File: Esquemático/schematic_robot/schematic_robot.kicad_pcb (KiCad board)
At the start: 2 copper layers, 19 parts, among them J1 Conn_01x04_Pin, J2 Conn_01x01_Socket, J3 Conn_01x01_Socket, J4 Conn_01x01_Socket, J5 Conn_01x01_Socket, J6 Conn_01x01_Socket, J7 Conn_01x01_Socket, J8 Conn_01x01_Socket, J9 Conn_01x01_Socket, M1 Motor_Servo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

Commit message: canseira
eu ein
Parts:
- moved J9 18.4 mm to (97.5, 109.0)
- moved J2 16.7 mm to (88.0, 93.0)
- moved J3 15.5 mm to (86.5, 108.0)
- moved J4 12.5 mm to (101.0, 91.0)
- moved J6 11.6 mm to (100.0, 99.0)
- moved J7 8.66 mm to (114.0, 115.0)
- moved J5 7.83 mm to (105.0, 114.5)
- moved J8 4.14 mm to (112.0, 104.0)
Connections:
- net +12V renamed 12V
- J3 pad 1: Net-(J3-Pin_1) -> 5V
- J8 pad 1: Net-(J8-Pin_1) -> 5V
- M1 pad 2: Net-(J3-Pin_1) -> 5V
- M2 pad 2: Net-(J3-Pin_1) -> 5V
- M3 pad 2: Net-(J3-Pin_1) -> 5V
- M4 pad 2: Net-(J3-Pin_1) -> 5V
- M5 pad 2: Net-(J3-Pin_1) -> 5V
- R1 pad 1: +5V -> 5V
- R2 pad 1: +5V -> 5V
- U2 pad 2: Net-(J8-Pin_1) -> 5V
- U3 pad 14: +5V -> 5V

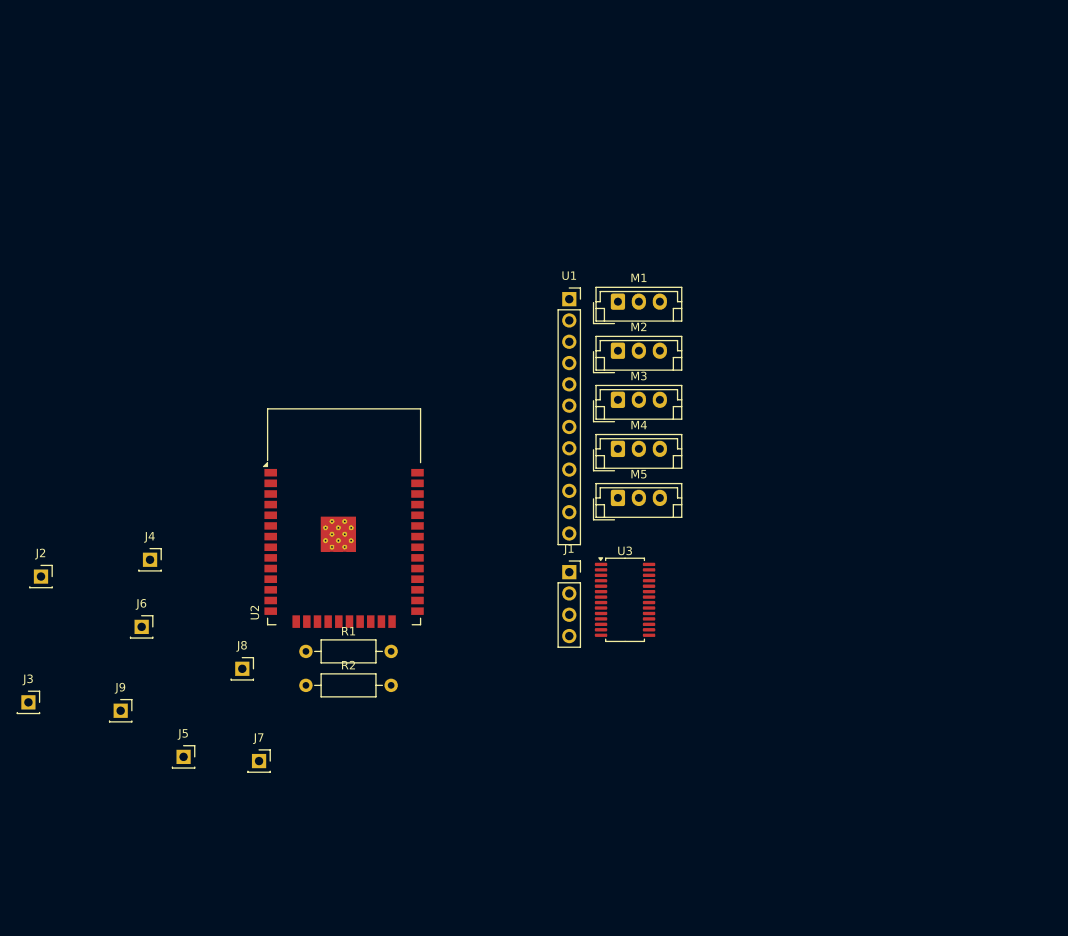
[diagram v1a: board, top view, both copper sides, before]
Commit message: Atualização do esquemático e datasheets, exclusão da pasta src
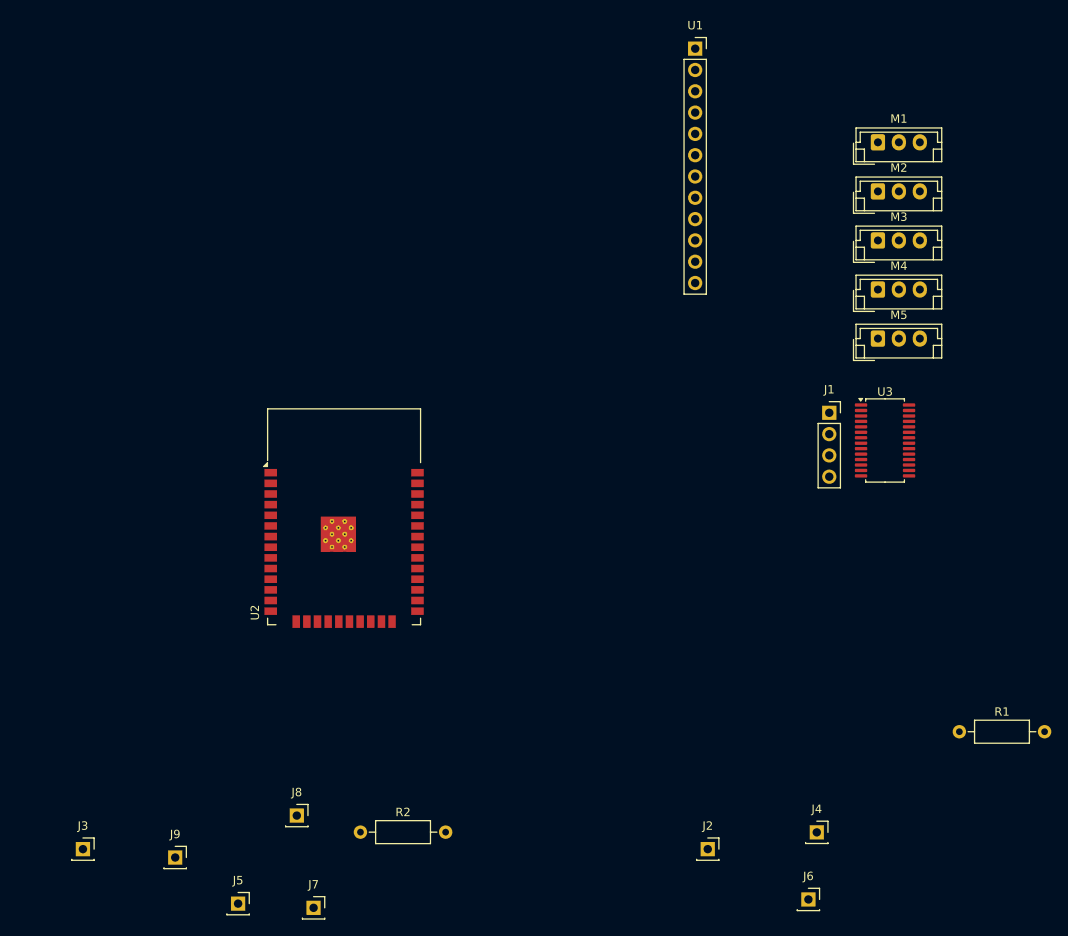
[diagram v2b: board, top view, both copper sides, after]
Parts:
- moved J2 85.9 mm to (167.5, 125.5)
- moved J4 85.9 mm to (180.5, 123.5)
- moved J6 85.9 mm to (179.5, 131.5)
- moved R1 78.5 mm to (197.5, 111.5)
- moved J1 36.4 mm to (182.0, 73.5)
- moved M1 36.4 mm to (187.8, 41.2)
- moved M2 36.4 mm to (187.8, 47.1)
- moved M3 36.4 mm to (187.8, 52.9)
- moved M4 36.4 mm to (187.8, 58.8)
- moved M5 36.4 mm to (187.8, 64.6)
- moved U3 36.4 mm to (188.6, 76.8)
- moved U1 33.4 mm to (166.0, 30.1)
- moved J3 18.7 mm to (93.0, 125.5)
- moved J5 18.7 mm to (111.5, 132.0)
- moved J7 18.7 mm to (120.5, 132.5)
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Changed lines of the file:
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@@
 	(footprint "Connector_PinSocket_2.54mm:PinSocket_1x12_P2.54mm_Vertical"
 		(layer "F.Cu")
-		(at 150.9875 59.925)
+		(at 166 30.06)
 		(descr "Through hole straight socket strip, 1x12, 2.54mm pitch, single row (from Kicad 4.0.7), script generated")
 		(tags "Through hole socket strip THT 1x12 2.54mm single row")
@@
 	(footprint "Package_SO:TSSOP-28_4.4x9.7mm_P0.65mm"
 		(layer "F.Cu")
-		(at 157.6375 95.775)
+		(at 188.6375 76.775)
 		(descr "TSSOP, 28 Pin (JEDEC MO-153 Var AE https://www.jedec.org/document_search?search_api_views_fulltext=MO-153), generated with kicad-footprint-generator ipc_gullwing_generator.py")
 		(tags "TSSOP SO")
@@
 	(footprint "Connector_JST:JST_EH_B3B-EH-A_1x03_P2.50mm_Vertical"
 		(layer "F.Cu")
-		(at 156.7875 60.225)
+		(at 187.7875 41.225)
 		(descr "JST EH series connector, B3B-EH-A (http://www.jst-mfg.com/product/pdf/eng/eEH.pdf), generated with kicad-footprint-generator")
 		(tags "connector JST EH vertical")
@@
 	(footprint "Connector_PinSocket_2.54mm:PinSocket_1x01_P2.54mm_Vertical"
 		(layer "F.Cu")
-		(at 101 91)
+		(at 180.5 123.5)
 		(descr "Through hole straight socket strip, 1x01, 2.54mm pitch, single row (from Kicad 4.0.7), script generated")
 		(tags "Through hole socket strip THT 1x01 2.54mm single row")
@@
 	(footprint "Connector_JST:JST_EH_B3B-EH-A_1x03_P2.50mm_Vertical"
 		(layer "F.Cu")
-		(at 156.7875 66.075)
+		(at 187.7875 47.075)
 		(descr "JST EH series connector, B3B-EH-A (http://www.jst-mfg.com/product/pdf/eng/eEH.pdf), generated with kicad-footprint-generator")
 		(tags "connector JST EH vertical")
@@
 	(footprint "Connector_PinSocket_2.54mm:PinSocket_1x01_P2.54mm_Vertical"
 		(layer "F.Cu")
-		(at 88 93)
+		(at 167.5 125.5)
 		(descr "Through hole straight socket strip, 1x01, 2.54mm pitch, single row (from Kicad 4.0.7), script generated")
 		(tags "Through hole socket strip THT 1x01 2.54mm single row")
@@
 	(footprint "Connector_JST:JST_EH_B3B-EH-A_1x03_P2.50mm_Vertical"
 		(layer "F.Cu")
-		(at 156.7875 71.925)
+		(at 187.7875 52.925)
 		(descr "JST EH series connector, B3B-EH-A (http://www.jst-mfg.com/product/pdf/eng/eEH.pdf), generated with kicad-footprint-generator")
 		(tags "connector JST EH vertical")
@@
 	(footprint "Connector_JST:JST_EH_B3B-EH-A_1x03_P2.50mm_Vertical"
 		(layer "F.Cu")
-		(at 156.7875 77.775)
+		(at 187.7875 58.775)
 		(descr "JST EH series connector, B3B-EH-A (http://www.jst-mfg.com/product/pdf/eng/eEH.pdf), generated with kicad-footprint-generator")
 		(tags "connector JST EH vertical")
@@
 	(footprint "Resistor_THT:R_Axial_DIN0207_L6.3mm_D2.5mm_P10.16mm_Horizontal"
 		(layer "F.Cu")
-		(at 119.5875 101.925)
+		(at 197.5 111.5)
 		(descr "Resistor, Axial_DIN0207 series, Axial, Horizontal, pin pitch=10.16mm, 0.25W = 1/4W, length*diameter=6.3*2.5mm^2, http://cdn-reichelt.de/documents/datenblatt/B400/1_4W%23YAG.pdf")
 		(tags "Resistor Axial_DIN0207 series Axial Horizontal pin pitch 10.16mm 0.25W = 1/4W length 6.3mm diameter 2.5mm")
@@
 	(footprint "Connector_PinSocket_2.54mm:PinSocket_1x01_P2.54mm_Vertical"
 		(layer "F.Cu")
-		(at 97.5 109)
+		(at 104 126.5)
 		(descr "Through hole straight socket strip, 1x01, 2.54mm pitch, single row (from Kicad 4.0.7), script generated")
 		(tags "Through hole socket strip THT 1x01 2.54mm single row")
@@
 	(footprint "Connector_PinSocket_2.54mm:PinSocket_1x04_P2.54mm_Vertical"
 		(layer "F.Cu")
-		(at 150.9875 92.475)
+		(at 181.9875 73.475)
 		(descr "Through hole straight socket strip, 1x04, 2.54mm pitch, single row (from Kicad 4.0.7), script generated")
 		(tags "Through hole socket strip THT 1x04 2.54mm single row")
@@
 	(footprint "Connector_PinSocket_2.54mm:PinSocket_1x01_P2.54mm_Vertical"
 		(layer "F.Cu")
-		(at 100 99)
+		(at 179.5 131.5)
 		(descr "Through hole straight socket strip, 1x01, 2.54mm pitch, single row (from Kicad 4.0.7), script generated")
 		(tags "Through hole socket strip THT 1x01 2.54mm single row")
@@
 	(footprint "Connector_PinSocket_2.54mm:PinSocket_1x01_P2.54mm_Vertical"
 		(layer "F.Cu")
-		(at 105 114.5)
+		(at 111.5 132)
 		(descr "Through hole straight socket strip, 1x01, 2.54mm pitch, single row (from Kicad 4.0.7), script generated")
 		(tags "Through hole socket strip THT 1x01 2.54mm single row")
@@
 	(footprint "Connector_JST:JST_EH_B3B-EH-A_1x03_P2.50mm_Vertical"
 		(layer "F.Cu")
-		(at 156.7875 83.625)
+		(at 187.7875 64.625)
 		(descr "JST EH series connector, B3B-EH-A (http://www.jst-mfg.com/product/pdf/eng/eEH.pdf), generated with kicad-footprint-generator")
 		(tags "connector JST EH vertical")
@@
 	(footprint "Connector_PinSocket_2.54mm:PinSocket_1x01_P2.54mm_Vertical"
 		(layer "F.Cu")
-		(at 114 115)
+		(at 120.5 132.5)
 		(descr "Through hole straight socket strip, 1x01, 2.54mm pitch, single row (from Kicad 4.0.7), script generated")
 		(tags "Through hole socket strip THT 1x01 2.54mm single row")
@@
 	(footprint "Connector_PinSocket_2.54mm:PinSocket_1x01_P2.54mm_Vertical"
 		(layer "F.Cu")
-		(at 86.5 108)
+		(at 93 125.5)
 		(descr "Through hole straight socket strip, 1x01, 2.54mm pitch, single row (from Kicad 4.0.7), script generated")
 		(tags "Through hole socket strip THT 1x01 2.54mm single row")
@@
 	(footprint "Resistor_THT:R_Axial_DIN0207_L6.3mm_D2.5mm_P10.16mm_Horizontal"
 		(layer "F.Cu")
-		(at 119.5875 105.975)
+		(at 126.0875 123.475)
 		(descr "Resistor, Axial_DIN0207 series, Axial, Horizontal, pin pitch=10.16mm, 0.25W = 1/4W, length*diameter=6.3*2.5mm^2, http://cdn-reichelt.de/documents/datenblatt/B400/1_4W%23YAG.pdf")
 		(tags "Resistor Axial_DIN0207 series Axial Horizontal pin pitch 10.16mm 0.25W = 1/4W length 6.3mm diameter 2.5mm")
@@
 	(footprint "Connector_PinSocket_2.54mm:PinSocket_1x01_P2.54mm_Vertical"
 		(layer "F.Cu")
-		(at 112 104)
+		(at 118.5 121.5)
 		(descr "Through hole straight socket strip, 1x01, 2.54mm pitch, single row (from Kicad 4.0.7), script generated")
 		(tags "Through hole socket strip THT 1x01 2.54mm single row")
